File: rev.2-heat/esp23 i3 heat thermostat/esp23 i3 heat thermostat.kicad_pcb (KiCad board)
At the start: 2 copper layers, 67 parts, among them J1 Conn_01x06, J2 bme280, J3 Conn_02x05_Odd_Even, J4 Conn_02x03_Odd_Even, Q1 BT134-600, Q2 BT134-600, SW1 SW_Push, SW2 SW_MEC_5E, SW3 SW_MEC_5E, SW4 SW_MEC_5E, SW5 SW_MEC_5E, U1 MAX7219, U2 MOC3063M, U3 MOC3063M, U4 ESP32-WROOM-32U, U5 LD1117S33TR_SOT223, U6 YAAJ_DCDC_StepDown_LM2596

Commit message: layout attempt 1
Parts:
- removed C2: 0.1uF, Capacitor_SMD:C_0603_1608Metric
- removed C4: 1nF, Capacitor_SMD:C_0603_1608Metric
- removed D1: heat, LED_SMD:LED_0603_1608Metric
- removed D2: fan, LED_SMD:LED_0603_1608Metric
- removed D7: RED LED, LED_SMD:LED_0603_1608Metric
- removed J3: Conn_02x05_Odd_Even, Connector_PinHeader_2.54mm:PinHeader_2x05_P2.54mm_Horizontal
- removed R10, R11, R13: 10K, Resistor_SMD:R_0603_1608Metric
- removed R12: 2.2K, Resistor_SMD:R_0603_1608Metric
- removed R2, R3: 560, Resistor_SMD:R_0603_1608Metric
- removed SW1: SW_Push, Button_Switch_THT:SW_Tactile_SPST_Angled_PTS645Vx39-2LFS
- C7, D3, D4, D5, D6, U4, U6: moved to B.Cu
- moved C10 346.3 mm to (113.5, 61.7), turned to -90 degrees
- moved R15 325.0 mm to (135.9, 111.0), turned to 90 degrees
- moved C8 324.7 mm to (129.5, 68.6), turned to -90 degrees
- moved R17 320.0 mm to (141.5, 111.0), turned to 90 degrees
- moved C11 305.1 mm to (124.0, 89.2), turned to -90 degrees
- moved R19 305.0 mm to (127.8, 106.2), turned to 180 degrees
- moved R18 285.8 mm to (153.2, 92.5), turned to 180 degrees
- moved U1 283.8 mm to (118.1, 100.6)
- moved C6 283.0 mm to (134.6, 85.6), turned to 180 degrees
- moved R20 278.6 mm to (127.8, 87.4)
- moved D5 276.0 mm to (133.9, 61.7), turned to 180 degrees
- moved R8 274.6 mm to (134.4, 93.5), turned to 180 degrees
- moved R7 268.8 mm to (143.3, 77.0), turned to 90 degrees
- moved R1 264.2 mm to (126.5, 100.6), turned to -90 degrees
- moved U2 254.0 mm to (129.6, 74.4)
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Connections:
- U4 pad 2: /VDD3V3 -> +3V3
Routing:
- net /F: track 0.00 -> 204.5 mm, vias 0 -> 5
- net /A: track 0.00 -> 203.1 mm, vias 0 -> 5
- net /G: track 0.00 -> 202.8 mm, vias 0 -> 4
- net /B: track 0.00 -> 195.3 mm, vias 0 -> 5
- net +5V: track 0.00 -> 194.6 mm, vias 0 -> 2
- net /E: track 0.00 -> 181.5 mm, vias 0 -> 5
- net /D: track 0.00 -> 179.3 mm, vias 0 -> 5
- net /C: track 0.00 -> 174.0 mm, vias 0 -> 5
- net /DP: track 0.00 -> 171.2 mm, vias 0 -> 5
- net +3V3: track 0.00 -> 104.1 mm, vias 0 -> 1
- net /D8: track 0.00 -> 92.0 mm, vias 0 -> 2
- net /D7: track 0.00 -> 77.2 mm, vias 0 -> 2
- net /ESP_IO25: track 0.00 -> 72.3 mm, vias 0 -> 4
- net /D6: track 0.00 -> 69.2 mm, vias 0 -> 2
- net /D4: track 0.00 -> 68.7 mm, vias 0 -> 1
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- added copper zone on B.Cu, net GND
- added copper zone on F.Cu, net GND
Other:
- board outline added: 111 x 65 mm

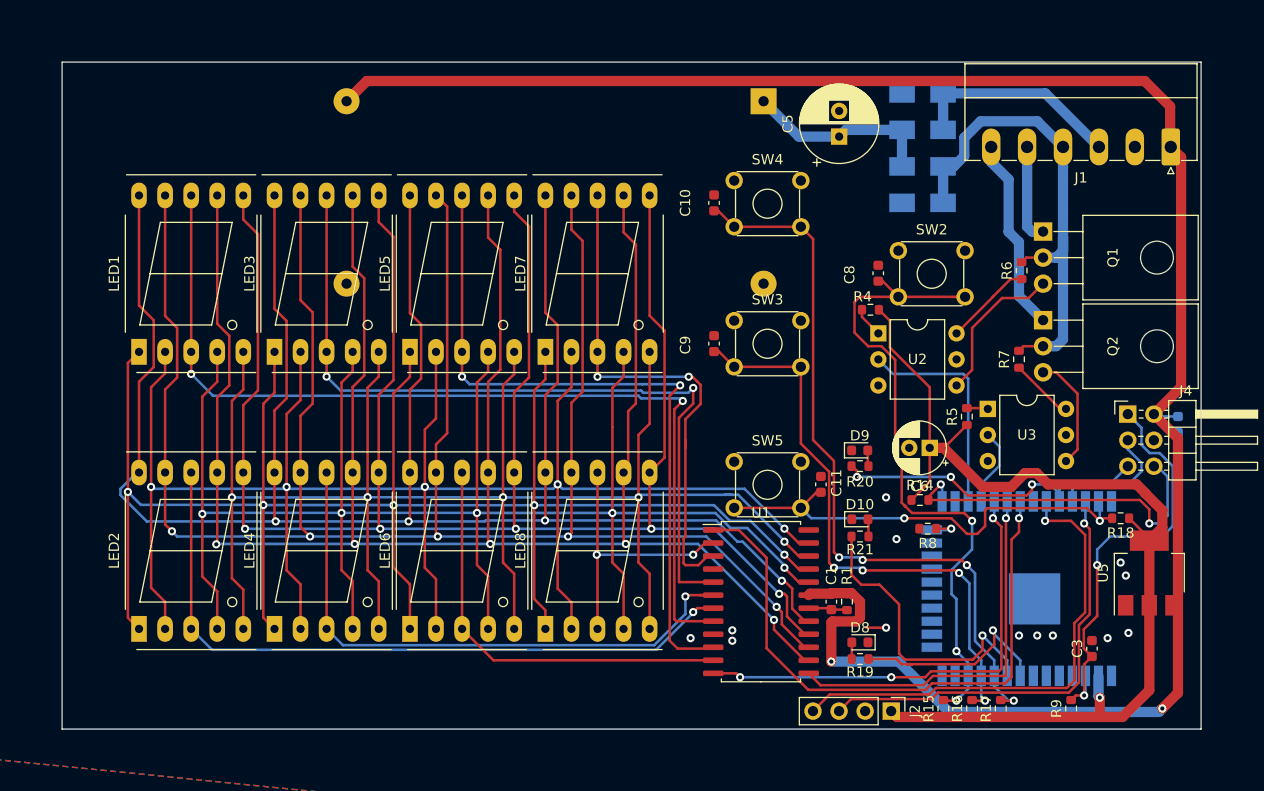
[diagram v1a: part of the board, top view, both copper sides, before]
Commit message: added mounting holes
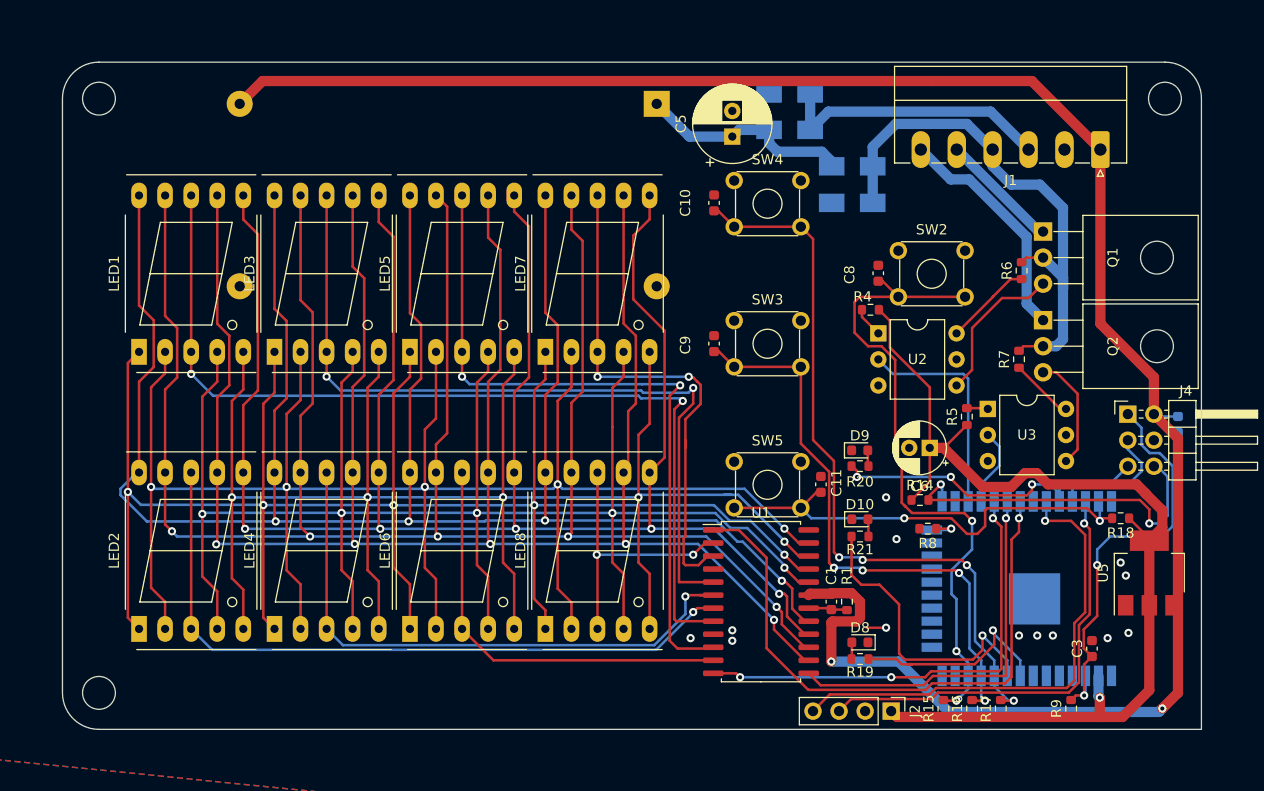
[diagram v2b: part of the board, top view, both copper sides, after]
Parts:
- added REF**: MountingHole_3.2mm_M3, MountingHole:MountingHole_3.2mm_M3, F.Cu at (53.6, 51.6)
- added REF**: MountingHole_3.2mm_M3, MountingHole:MountingHole_3.2mm_M3, F.Cu at (157.5, 51.6)
- added REF**: MountingHole_3.2mm_M3, MountingHole:MountingHole_3.2mm_M3, F.Cu at (53.6, 109.5)
- moved D4 13.0 mm to (120.9, 54.6)
- moved D6 13.0 mm to (120.9, 51.1)
- moved U6 10.4 mm to (108.0, 52.1)
- moved C5 10.4 mm to (115.3, 55.3)
- moved J1 6.86 mm to (151.2, 56.5)
- moved D3 6.86 mm to (127.0, 58.2)
- moved D5 6.86 mm to (127.0, 61.7)
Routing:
- net /common: track 20.9 -> 27.1 mm
- net /Hot: track 48.5 -> 53.0 mm
- net /Fan: track 19.0 -> 22.6 mm
- net +24V: track 18.7 -> 21.2 mm
- net /Heat: track 9.52 -> 11.7 mm
- net +5V: track 194.6 -> 196.5 mm
- net /B: track 195.3 -> 196.6 mm
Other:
- outline, holes or cut-outs redrawn

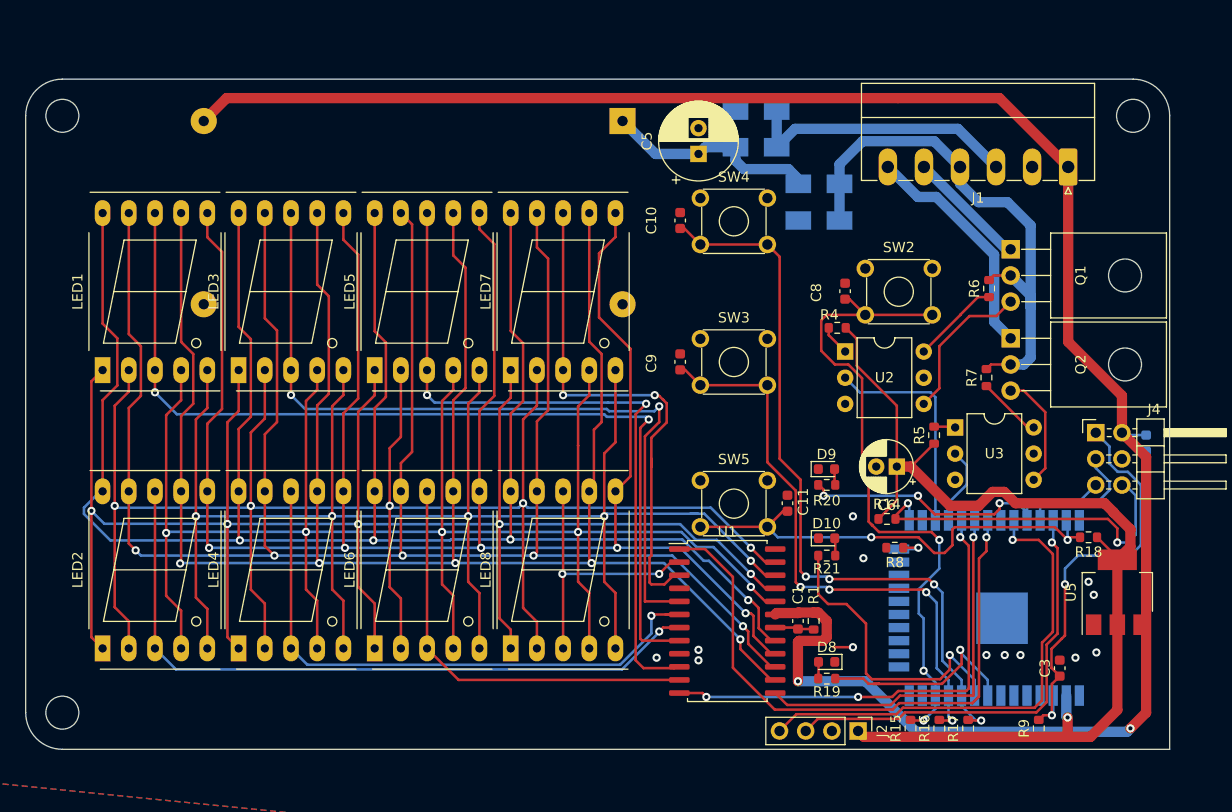
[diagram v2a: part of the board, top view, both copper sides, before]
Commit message: add fourth corner hole
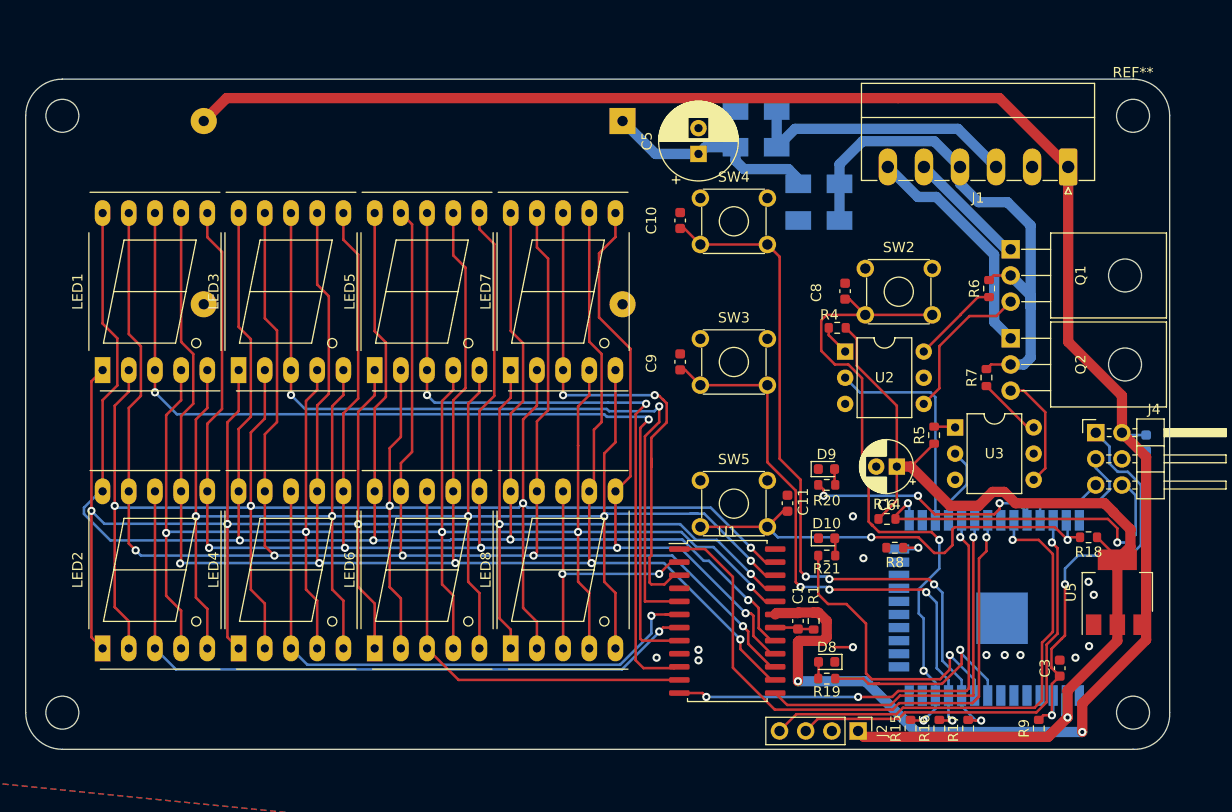
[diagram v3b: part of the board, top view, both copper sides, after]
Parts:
- added REF**: MountingHole_3.2mm_M3, MountingHole:MountingHole_3.2mm_M3, F.Cu at (157.5, 51.6)
- moved REF** 57.9 mm to (157.5, 109.5)
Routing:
- net +3V3: track 104.1 -> 99.7 mm
- net +5V: track 196.5 -> 193.9 mm
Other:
- outline, holes or cut-outs redrawn
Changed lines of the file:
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@@
     )
     (pad_to_mask_clearance 0)
+    (grid_origin 132.7912 114.1984)
     (pcbplotparams
       (layerselection 0x00010fc_ffffffff)
@@
   )
   (footprint "MountingHole:MountingHole_3.2mm_M3" (layer "F.Cu")
-    (at 157.48 51.562)
+    (at 157.48 109.474)
     (descr "Mounting Hole 3.2mm, no annular, M3")
     (tags "mounting hole 3.2mm no annular m3")
@@
     )
   )
+  (footprint "MountingHole:MountingHole_3.2mm_M3" (layer "F.Cu")
+    (at 157.48 51.562)
+    (descr "Mounting Hole 3.2mm, no annular, M3")
+    (tags "mounting hole 3.2mm no annular m3")
+    (attr exclude_from_pos_files exclude_from_bom)
+    (fp_text reference "REF**" (at 0 -4.2) (layer "F.SilkS")
+      (effects (font (size 1 1) (thickness 0.15)))
+    )
+    (fp_text value "MountingHole_3.2mm_M3" (at 0 4.2) (layer "F.Fab")
+      (effects (font (size 1 1) (thickness 0.15)))
+    )
+    (fp_text user "${REFERENCE}" (at 0 0) (layer "F.Fab")
+      (effects (font (size 1 1) (thickness 0.15)))
+    )
+    (fp_circle (center 0 0) (end 3.2 0) (layer "Cmts.User") (width 0.15) (fill none))
+    (fp_circle (center 0 0) (end 3.45 0) (layer "F.CrtYd") (width 0.05) (fill none))
+    (pad "" np_thru_hole circle (at 0 0) (size 3.2 3.2) (drill 3.2) (layers *.Cu *.Mask))
+  )
   (footprint "Package_SO:SOP-24_7.5x15.4mm_P1.27mm" (layer "F.Cu")
     (at 118.11 100.584)
@@
   )
   (gr_arc (start 50.038 51.562) (mid 51.079528 49.047528) (end 53.594 48.006) (layer "Edge.Cuts") (width 0.1))
-  (gr_line (start 161.036 113.03) (end 161.036 51.562) (layer "Edge.Cuts") (width 0.1))
+  (gr_line (start 161.036 109.474) (end 161.036 51.562) (layer "Edge.Cuts") (width 0.1))
   (gr_arc (start 157.48 48.006) (mid 159.994472 49.047528) (end 161.036 51.562) (layer "Edge.Cuts") (width 0.1))
+  (gr_arc (start 161.036 109.474) (mid 160.045901 112.039901) (end 157.48 113.03) (layer "Edge.Cuts") (width 0.1))
   (gr_line (start 157.48 48.006) (end 53.594 48.006) (layer "Edge.Cuts") (width 0.1))
-  (gr_line (start 53.594 113.03) (end 161.036 113.03) (layer "Edge.Cuts") (width 0.1))
+  (gr_line (start 53.594 113.03) (end 157.48 113.03) (layer "Edge.Cuts") (width 0.1))
   (gr_line (start 50.038 51.562) (end 50.038 109.474) (layer "Edge.Cuts") (width 0.1))
   (gr_arc (start 53.594 113.03) (mid 51.079528 111.988472) (end 50.038 109.474) (layer "Edge.Cuts") (width 0.1))
   (segment (start 122.9 99.809) (end 122.76 99.949) (width 1) (layer "F.Cu") (net 1))
-  (segment (start 158.75 84.659) (end 158.75 109.474) (width 1) (layer "F.Cu") (net 1))
+  (segment (start 156.402 82.311) (end 158.75 84.659) (width 1) (layer "F.Cu") (net 1))
   (segment (start 151.189 56.5265) (end 144.508989 49.846489) (width 1) (layer "F.Cu") (net 1))
   (segment (start 144.508989 49.846489) (end 134.682489 49.846489) (width 1) (layer "F.Cu") (net 1))
@@
   (segment (start 151.189 73.499726) (end 151.189 56.5265) (width 1) (layer "F.Cu") (net 1))
   (segment (start 127.762 100.584) (end 126.937 99.759) (width 1) (layer "F.Cu") (net 1))
-  (segment (start 156.402 82.311) (end 158.75 84.659) (width 1) (layer "F.Cu") (net 1))
   (segment (start 125.018 99.759) (end 124.968 99.809) (width 1) (layer "F.Cu") (net 1))
   (segment (start 69.533511 49.846489) (end 67.31 52.07) (width 1) (layer "F.Cu") (net 1))
   (segment (start 156.402 78.712726) (end 151.189 73.499726) (width 1) (layer "F.Cu") (net 1))
+  (segment (start 152.5524 108.6104) (end 152.5524 111.3536) (width 1) (layer "F.Cu") (net 1))
   (segment (start 124.968 99.809) (end 122.9 99.809) (width 1) (layer "F.Cu") (net 1))
   (segment (start 134.682489 49.846489) (end 69.533511 49.846489) (width 1) (layer "F.Cu") (net 1))
+  (segment (start 158.75 84.659) (end 158.75 102.4128) (width 1) (layer "F.Cu") (net 1))
   (segment (start 127.40052 102.50852) (end 127.762 102.14704) (width 1) (layer "F.Cu") (net 1))
+  (segment (start 158.75 102.4128) (end 152.5524 108.6104) (width 1) (layer "F.Cu") (net 1))
   (segment (start 125.07548 102.50852) (end 127.40052 102.50852) (width 1) (layer "F.Cu") (net 1))
   (segment (start 124.968 102.616) (end 125.07548 102.50852) (width 1) (layer "F.Cu") (net 1))
   (segment (start 126.492 99.759) (end 125.018 99.759) (width 1) (layer "F.Cu") (net 1))
-  (segment (start 158.75 109.474) (end 157.226 110.998) (width 1) (layer "F.Cu") (net 1))
   (segment (start 156.402 82.311) (end 156.402 78.712726) (width 1) (layer "F.Cu") (net 1))
   (segment (start 126.937 99.759) (end 126.492 99.759) (width 1) (layer "F.Cu") (net 1))
   (segment (start 124.968 106.426) (end 124.968 102.616) (width 1) (layer "F.Cu") (net 1))
   (via (at 124.968 106.426) (size 0.8) (drill 0.4) (layers "F.Cu" "B.Cu") (net 1))
-  (via (at 157.226 110.998) (size 0.8) (drill 0.4) (layers "F.Cu" "B.Cu") (net 1))
-  (segment (start 158.75 82.537) (end 156.628 82.537) (width 0.25) (layer "B.Cu") (net 1))
-  (segment (start 157.226 110.998) (end 156.888489 111.335511) (width 1) (layer "B.Cu") (net 1))
+  (via (at 152.5524 111.3536) (size 0.8) (drill 0.4) (layers "F.Cu" "B.Cu") (net 1))
   (segment (start 131.525978 106.426) (end 124.968 106.426) (width 1) (layer "B.Cu") (net 1))
-  (segment (start 136.435489 111.335511) (end 131.525978 106.426) (width 1) (layer "B.Cu") (net 1))
+  (segment (start 152.5524 111.3536) (end 136.453578 111.3536) (width 1) (layer "B.Cu") (net 1))
+  (segment (start 158.75 82.537) (end 156.628 82.537) (width 0.25) (layer "B.Cu") (net 1))
+  (segment (start 136.453578 111.3536) (end 131.525978 106.426) (width 1) (layer "B.Cu") (net 1))
   (segment (start 156.628 82.537) (end 156.402 82.311) (width 0.25) (layer "B.Cu") (net 1))
-  (segment (start 156.888489 111.335511) (end 136.435489 111.335511) (width 1) (layer "B.Cu") (net 1))
   (segment (start 126.442 101.359) (end 126.492 101.409) (width 0.25) (layer "F.Cu") (net 2))
   (segment (start 124.828 101.219) (end 124.968 101.359) (width 0.25) (layer "F.Cu") (net 2))
@@
   (via (at 131.318 94.488) (size 0.8) (drill 0.4) (layers "F.Cu" "B.Cu") (free) (net 3))
   (via (at 153.162 96.774) (size 0.8) (drill 0.4) (layers "F.Cu" "B.Cu") (free) (net 3))
-  (via (at 153.924 103.632) (size 0.8) (drill 0.4) (layers "F.Cu" "B.Cu") (free) (net 3))
+  (via (at 153.2128 103.0224) (size 0.8) (drill 0.4) (layers "F.Cu" "B.Cu") (free) (net 3))
   (via (at 151.892 104.14) (size 0.8) (drill 0.4) (layers "F.Cu" "B.Cu") (free) (net 3))
   (via (at 130.302 90.424) (size 0.8) (drill 0.4) (layers "F.Cu" "B.Cu") (free) (net 3))
@@
   (segment (start 129.603 72.136) (end 130.674511 73.207511) (width 0.25) (layer "F.Cu") (net 6))
   (segment (start 134.559113 85.598) (end 135.953 85.598) (width 0.25) (layer "F.Cu") (net 6))
+  (segment (start 155.956 100.94) (end 155.956 102.5144) (width 1) (layer "F.Cu") (net 6))
   (segment (start 148.336 111.823) (end 135.89 111.823) (width 1) (layer "F.Cu") (net 6))
   (segment (start 135.89 111.823) (end 131.371 111.823) (width 1) (layer "F.Cu") (net 6))
@@
   (segment (start 135.953 85.598) (end 138.176 83.375) (width 0.25) (layer "F.Cu") (net 6))
   (segment (start 155.590659 90.027341) (end 155.590659 90.058659) (width 1) (layer "F.Cu") (net 6))
-  (segment (start 151.13 109.941) (end 151.13 111.632) (width 1) (layer "F.Cu") (net 6))
   (segment (start 157.226 91.694) (end 157.226 93.37) (width 1) (layer "F.Cu") (net 6))
   (segment (start 155.590659 90.027341) (end 154.717319 89.154) (width 1) (layer "F.Cu") (net 6))
@@
   (segment (start 134.559113 85.598) (end 134.559113 88.897887) (width 0.25) (layer "F.Cu") (net 6))
   (segment (start 144.981433 88.054489) (end 143.847511 88.054489) (width 1) (layer "F.Cu") (net 6))
-  (segment (start 155.956 109.22) (end 153.353 111.823) (width 1) (layer "F.Cu") (net 6))
-  (segment (start 153.353 111.823) (end 151.321 111.823) (width 1) (layer "F.Cu") (net 6))
+  (segment (start 151.13 107.3404) (end 151.13 109.941) (width 1) (layer "F.Cu") (net 6))
   (segment (start 146.080944 89.154) (end 144.981433 88.054489) (width 1) (layer "F.Cu") (net 6))
+  (segment (start 155.956 102.5144) (end 151.13 107.3404) (width 1) (layer "F.Cu") (net 6))
   (segment (start 131.371 111.823) (end 130.8 111.252) (width 1) (layer "F.Cu") (net 6))
-  (segment (start 151.13 111.632) (end 151.321 111.823) (width 1) (layer "F.Cu") (net 6))
+  (segment (start 149.248 111.823) (end 148.336 111.823) (width 1) (layer "F.Cu") (net 6))
   (segment (start 157.226 93.37) (end 155.956 94.64) (width 1) (layer "F.Cu") (net 6))
   (segment (start 135.920944 85.598) (end 134.559113 85.598) (width 1) (layer "F.Cu") (net 6))
@@
   (segment (start 142.49804 89.40396) (end 139.726904 89.40396) (width 1) (layer "F.Cu") (net 6))
   (segment (start 134.559113 79.695113) (end 134.559113 85.598) (width 0.25) (layer "F.Cu") (net 6))
-  (segment (start 155.956 100.94) (end 155.956 109.22) (width 1) (layer "F.Cu") (net 6))
-  (segment (start 151.321 111.823) (end 148.336 111.823) (width 1) (layer "F.Cu") (net 6))
+  (segment (start 151.13 109.941) (end 149.248 111.823) (width 1) (layer "F.Cu") (net 6))
   (segment (start 139.726904 89.40396) (end 135.920944 85.598) (width 1) (layer "F.Cu") (net 6))
   (segment (start 130.674511 73.207511) (end 130.674511 75.810511) (width 0.25) (layer "F.Cu") (net 6))

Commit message: generated gerbers
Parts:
- added G***: LOGO, Evan's misc parts:Evan Logo, F.Cu at (63.5, 108.8)
- added G***: LOGO, Evan's misc parts:OSHW gear, F.Cu at (60.9, 52.7)
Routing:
- net /common: track 27.1 -> 31.9 mm
- net /Hot: track 53.0 -> 50.8 mm
- net GND: track 1.91 -> 0.00 mm
- net /ESP_IO0: track 34.7 -> 32.8 mm
- net /D3: track 57.9 -> 56.6 mm
- net /ESP_EN: track 40.4 -> 39.4 mm
- net /Fan: track 22.6 -> 21.6 mm
- net /D5: track 50.2 -> 49.5 mm
- net /DP: track 171.2 -> 170.5 mm
- net /ESP_IO32: track 20.8 -> 20.3 mm
- net /ESP_IO27: track 64.4 -> 64.2 mm, vias 3 -> 2
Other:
- board text added: "21"
- board text added: "22"
- board text added: "3v3"
- board text added: "5v"
- board text added: "En"
- board text added: "IO0"
- board text added: "IO1"
- board text added: "IO3"
- board text added: "abzman2k.wordpress.com"
- board text added: "common"
- board text added: "down"
- board text added: "fan"
- board text added: "gnd"
- board text added: "heat"
- board text added: "heat onnly thermostat for i3detroit"
- board text added: "heating active"
- board text added: "hot"
- board text added: "off"
- board text added: "reset"
- board text added: "up"
